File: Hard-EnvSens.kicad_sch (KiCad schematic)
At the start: 32 parts, among them P1 USB_C_Plug_USB2.0, SW1 SW_Push, SW3 SW_Push, U1 LD1117S33TR_SOT223, U2 ESP32-C6-WROOM-1, U3 CP2104

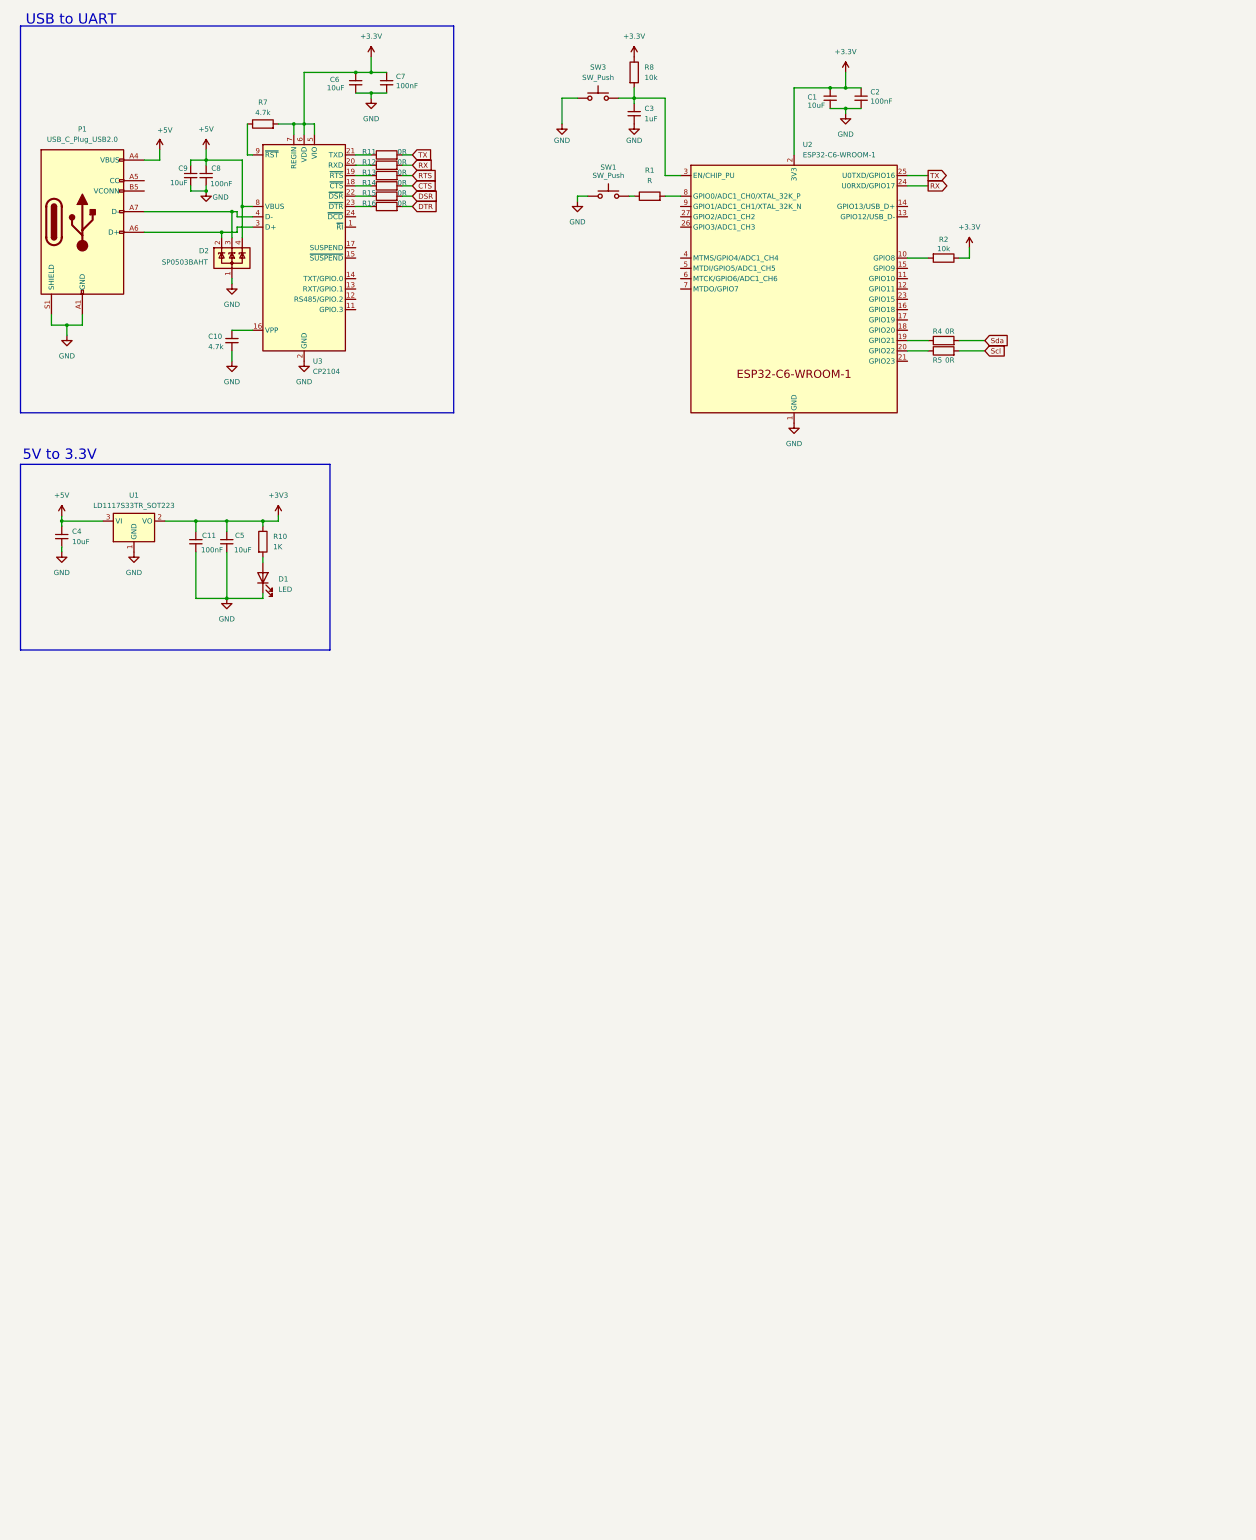
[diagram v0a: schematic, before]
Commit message: Added some sensors
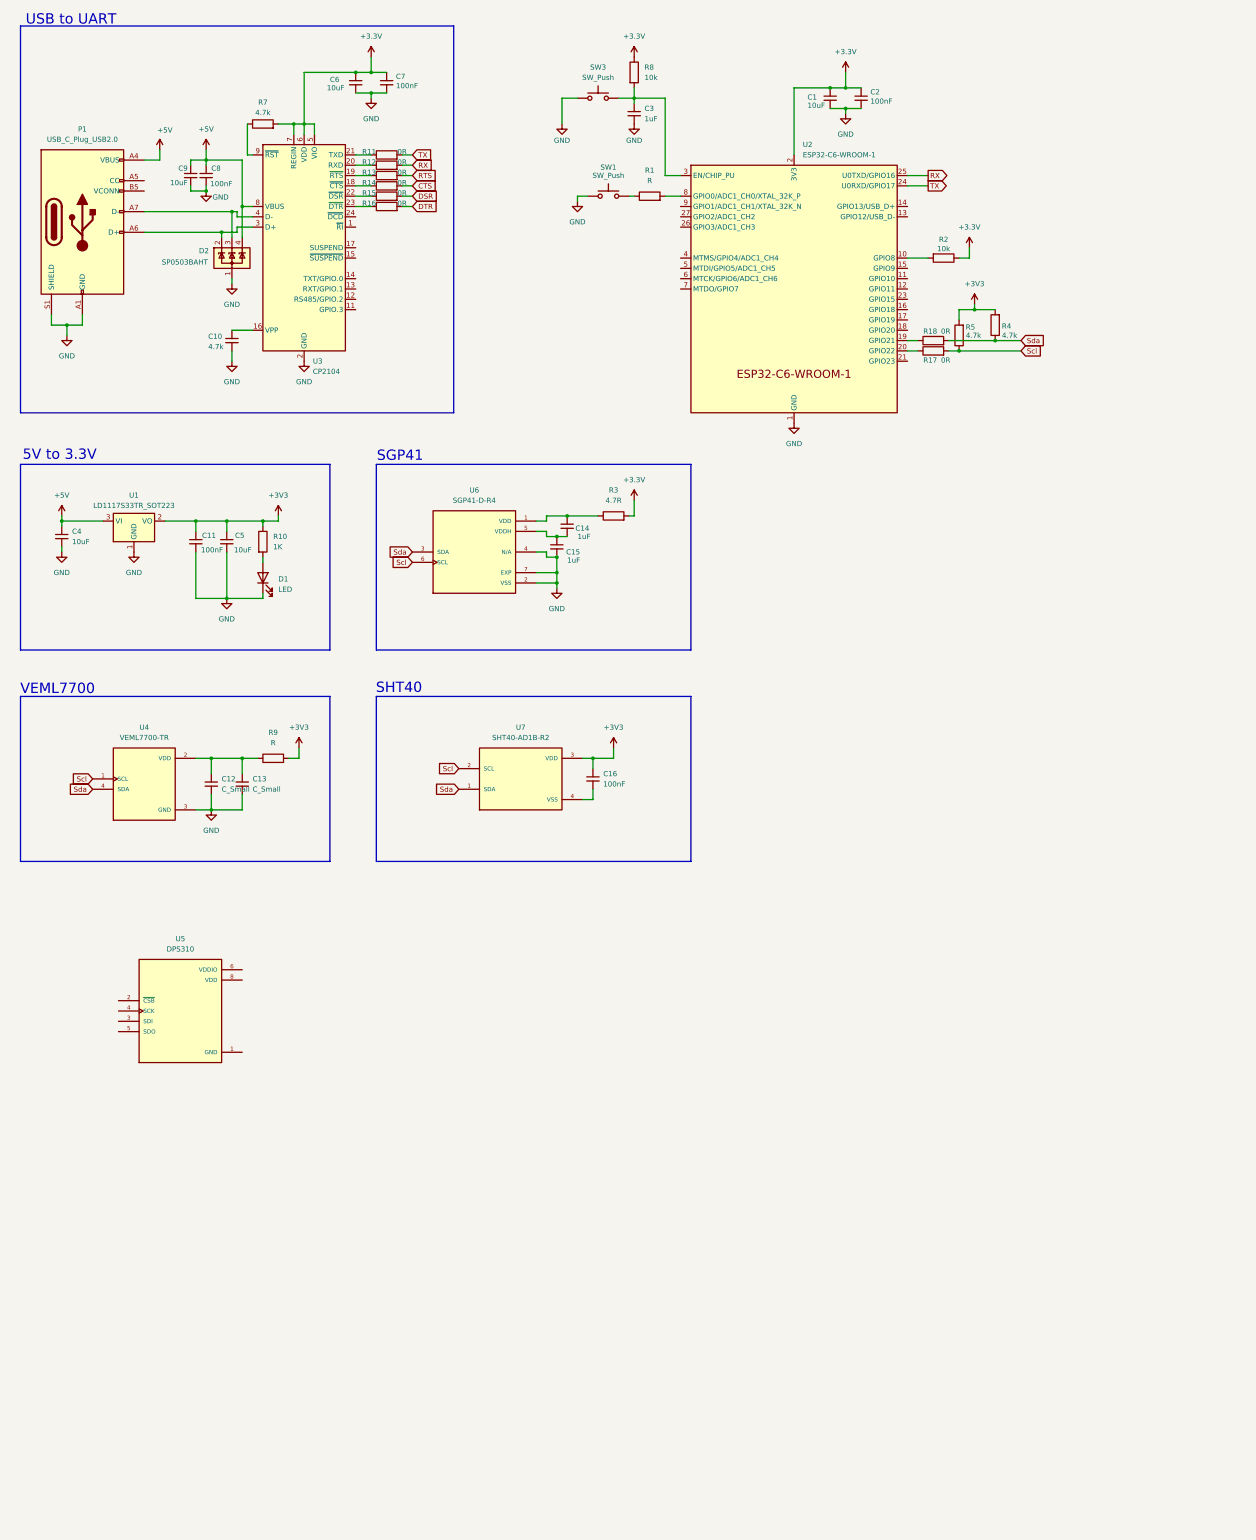
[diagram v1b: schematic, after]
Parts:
- added C12, C13: C_Small, symbol Device:C_Small
- added C14, C15: 1uF, symbol Device:C_Small
- added C16: 100nF, symbol Device:C_Small
- added R17, R18: 0R, symbol Device:R
- added R3: 4.7R, symbol Device:R
- added R9: R, symbol Device:R
- added U4: VEML7700-TR, VEML7700-TR:XDCR_VEML7700-TR, symbol VEML7700-TR:VEML7700-TR
- added U5: DPS310, DPS310:XDCR_DPS310, symbol DPS310:DPS310
- added U6: SGP41-D-R4, SGP41-D-R4:XDCR_SGP41-D-R4, symbol SGP41-D-R4:SGP41-D-R4
- added U7: SHT40-AD1B-R2, SHT40-AD1B-R2:SHT4X, symbol SHT40-AD1B-R2:SHT40-AD1B-R2
- R4, R5: value 0R -> 4.7k
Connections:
- net +3.3V: now also R3.2
- net +3V3: now also R4.2, R5.2, C16.1, R9.2, U7.3 (VDD)
- net GND: now also C12.2, C13.2, C15.2, U4.3 (GND), U5.1 (GND), U5.7 (GND), U6.2 (VSS), U6.4 (N/A), U6.7 (EXP)
- net RX: now also U2.25 (U0TXD/GPIO16); no longer U2.24 (U0RXD/GPIO17)
- net Scl: now also R5.1, R17.2, U4.1 (SCL), U6.6 (SCL), U7.2 (SCL); no longer R5.2
- net Sda: now also R4.1, R18.2, U4.4 (SDA), U6.3 (SDA), U7.1 (SDA); no longer R4.2
- net TX: now also U2.24 (U0RXD/GPIO17); no longer U2.25 (U0TXD/GPIO16)
- net at U2.20 (GPIO22): now also R17.1; no longer R5.1
- net at U2.19 (GPIO21): now also R18.1; no longer R4.1
- new net: C12.1, C13.1, R9.1, U4.2 (VDD)
- new net: C16.2, U7.4 (VSS)
- new net: C14.1, R3.1, U6.1 (VDD)
- new net: C14.2, C15.1, U6.5 (VDDH)
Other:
- note added: "SGP41"
- note added: "SHT40"
- note added: "VEML7700"
- moved on the sheet: R4, R5

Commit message: Dps368
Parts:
- removed R14, R16: 0R, symbol Device:R
- added C17: 10nF, symbol Device:C_Small
- added D3: SP0503BAHT, Package_TO_SOT_SMD:SOT-143, symbol Power_Protection:SP0503BAHT
- added D4: LED, symbol Device:LED
- added P2: USB_C_Plug_USB2.0, symbol Connector:USB_C_Plug_USB2.0
- added Q1, Q2: SS8050, Package_TO_SOT_SMD:SOT-23, symbol Transistor_BJT:SS8050
- added R19, R6: 12k, symbol Device:R
- R1: value R -> 10k
- R11, R12: value 0R -> 100R
- R13: value 0R -> 4.7k
- R9: value R -> 10R
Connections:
- net +3.3V: now also R1.1
- net +5V: now also D3.4 (K), P2.A4 (VBUS), P2.A9 (VBUS), P2.B4 (VBUS), P2.B9 (VBUS)
- net DTR: now also U3.23 (~{DTR}), Q2.2 (E), R6.2
- net GND: now also D3.1 (A), D4.1 (K), P2.A1 (GND), P2.A12 (GND), P2.B1 (GND), P2.B12 (GND), P2.S1 (SHIELD)
- net RTS: now also U3.19 (~{RTS}), Q1.2 (E), R19.1; no longer R13.2
- net EN: now reaches C3.1, R8.2, SW3.2, U2.3 (EN/CHIP_PU)
- net EN: now also Q1.3 (C)
- net at SW1.2: now also R1.2, U2.8 (GPIO0/ADC1_CH0/XTAL_32K_P); no longer R1.1
- net at C14.1, R3.1, U6.1 (VDD): now also C17.1
- net at R13.1: now also D4.2 (A); no longer U3.19 (~{RTS})
- net at C14.2, C15.1, U6.5 (VDDH): now also C17.2
- net D-: now reaches U2.13 (GPIO12/USB_D-)
- net D-: now also D3.3 (K), P2.A7 (D-)
- net D+: now reaches U2.14 (GPIO13/USB_D+)
- net D+: now also D3.2 (K), P2.A6 (D+)
- net IO9: now reaches U2.15 (GPIO9)
- net IO9: now also Q2.3 (C)
- net at U2.23 (GPIO15): now also R13.2
- new net: Q2.1 (B), R19.2
- new net: Q1.1 (B), R6.1
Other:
- moved on the sheet: C1, C11, C12, C13, C14, C15, C16, C2, C3, C4, C5, D1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

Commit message: dps368
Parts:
- removed U5: DPS310, DPS310:XDCR_DPS310, symbol DPS310:DPS310
- added C18, C19: 100nF, symbol Device:C_Small
- added U5: DPS368, DPS368:LGA8S145X65P2X4_200X250X110-V, symbol DPS368:DPS368
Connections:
- net GND: now also C18.2, C19.2, U5.1 (GND_1), U5.7 (GND_2)
- net Scl: now also U5.4 (SCK)
- net Sda: now also U5.3 (SDI)
- new net: C18.1, C19.1, U5.6 (VDDIO), U5.8 (VDD)
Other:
- note added: "Debug USB"
- moved on the sheet: D3, P2

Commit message: aa
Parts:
- added U8: AS7341-DLGT, AS7341-DLGT:PSON80P310X200X110-8N, symbol AS7341-DLGT:AS7341-DLGT
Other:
- note added: "DPS368"
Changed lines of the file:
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@@
 		)
 	)
+	(text "DPS368\n"
+		(exclude_from_sim no)
+		(at 31.496 291.338 0)
+		(effects
+			(font
+				(size 2.54 2.54)
+			)
+		)
+	)
 	(text "5V to 3.3V\n"
 		(exclude_from_sim no)
@@
 					(unit 1)
 				)
+			)
+		)
+	)
+	(symbol
+		(lib_id "AS7341-DLGT:AS7341-DLGT")
+		(at 148.59 314.96 0)
+		(unit 1)
+		(exclude_from_sim no)
+		(in_bom yes)
+		(on_board yes)
+		(dnp no)
+		(fields_autoplaced yes)
+		(property "Reference" "U8"
+			(at 148.59 297.18 0)
+			(effects
+				(font
+					(size 1.27 1.27)
+				)
+			)
+		)
+		(property "Value" "AS7341-DLGT"
+			(at 148.59 299.72 0)
+			(effects
+				(font
+					(size 1.27 1.27)
+				)
+			)
+		)
+		(property "Footprint" "AS7341-DLGT:PSON80P310X200X110-8N"
+			(at 148.59 314.96 0)
+			(effects
+				(font
+					(size 1.27 1.27)
+				)
+				(justify bottom)
+				(hide yes)
+			)
+		)
+		(property "Datasheet" ""
+			(at 148.59 314.96 0)
+			(effects
+				(font
+					(size 1.27 1.27)
+				)
+				(hide yes)
+			)
+		)
+		(property "Description" ""
+			(at 148.59 314.96 0)
+			(effects
+				(font
+					(size 1.27 1.27)
+				)
+				(hide yes)
+			)
+		)
+		(property "MF" "ams"
+			(at 148.59 314.96 0)
+			(effects
+				(font
+					(size 1.27 1.27)
+				)
+				(justify bottom)
+				(hide yes)
+			)
+		)
+		(property "MAXIMUM_PACKAGE_HEIGHT" "1.1 mm"
+			(at 148.59 314.96 0)
+			(effects
+				(font
+					(size 1.27 1.27)
+				)
+				(justify bottom)
+				(hide yes)
+			)
+		)
+		(property "Package" "TFLGA-8 ams"
+			(at 148.59 314.96 0)
+			(effects
+				(font
+					(size 1.27 1.27)
+				)
+				(justify bottom)
+				(hide yes)
+			)
+		)
+		(property "Price" "None"
+			(at 148.59 314.96 0)
+			(effects
+				(font
+					(size 1.27 1.27)
+				)
+				(justify bottom)
+				(hide yes)
+			)
+		)
+		(property "Check_prices" "https://www.snapeda.com/parts/AS7341-DLGT/ams/view-part/?ref=eda"
+			(at 148.59 314.96 0)
+			(effects
+				(font
+					(size 1.27 1.27)
+				)
+				(justify bottom)
+				(hide yes)
+			)
+		)
+		(property "STANDARD" "IPC7351B"
+			(at 148.59 314.96 0)
+			(effects
+				(font
+					(size 1.27 1.27)
+				)
+				(justify bottom)
+				(hide yes)
+			)
+		)
+		(property "PARTREV" "V3"
+			(at 148.59 314.96 0)
+			(effects
+				(font
+					(size 1.27 1.27)
+				)
+				(justify bottom)
+				(hide yes)
+			)
+		)
+		(property "SnapEDA_Link" "https://www.snapeda.com/parts/AS7341-DLGT/ams/view-part/?ref=snap"
+			(at 148.59 314.96 0)
+			(effects
+				(font
+					(size 1.27 1.27)
+				)
+				(justify bottom)
+				(hide yes)
+			)
+		)
+		(property "MP" "AS7341-DLGT"
+			(at 148.59 314.96 0)
+			(effects
+				(font
+					(size 1.27 1.27)
+				)
+				(justify bottom)
+				(hide yes)
+			)
+		)
+		(property "Description_1" "Optical Sensor Ambient - I²C 8-TFLGA"
+			(at 148.59 314.96 0)
+			(effects
+				(font
+					(size 1.27 1.27)
+				)
+				(justify bottom)
+				(hide yes)
+			)
+		)
+		(property "Availability" "In Stock"
+			(at 148.59 314.96 0)
+			(effects
+				(font
+					(size 1.27 1.27)
+				)
+				(justify bottom)
+				(hide yes)
+			)
+		)
+		(property "MANUFACTURER" "AMS"
+			(at 148.59 314.96 0)
+			(effects
+				(font
+					(size 1.27 1.27)
+				)
+				(justify bottom)
+				(hide yes)
+			)
+		)
+		(pin "2"
+		)
+		(pin "6"
+		)
+		(pin "4"
+		)
+		(pin "8"
+		)
+		(pin "5"
+		)
+		(pin "3"
+		)
+		(pin "1"
+		)
+		(pin "7"
+		)
+		(instances
+			(project ""
+				(path "/08245449-9253-4ad9-82ff-78abebb7792e"
+					(reference "U8")
+					(unit 1)
+				)

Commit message: New sensors
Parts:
- removed R15: 0R, symbol Device:R
- added C20: 0.1uF, symbol Device:C_Small
- added C21: 0.01uF, symbol Device:C_Small
- added C22: 10uF, symbol Device:C_Small
- added C23: 100nF, symbol Device:C_Small
- added C24: 4.7uF, symbol Device:C_Small
- added R14: 10k, symbol Device:R
- added U9: TPS79318DBVTG4, TPS79318DBVTG4:SOT95P280X145-5N, symbol TPS793-18:TPS79318DBVTG4
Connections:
- net +5V: now also C20.1, U9.1 (IN), U9.3 (EN)
- net GND: now also U8.3 (GND), U8.5 (PGND), C20.2, C21.2, C22.2, C23.2, C24.2, U9.2 (GND)
- net Scl: now also U8.2 (SCL)
- net Sda: now also U8.8 (SDA)
- net 1.8v: now reaches U8.1 (VDD)
- net 1.8v: now also C22.1, C23.1, C24.1, R14.2, U9.5 (OUT)
- net at U8.7 (INT): now also R14.1
- new net: C21.1, U9.4 (NR)
- no-connect marks 0 -> 31
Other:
- moved on the sheet: C14, C15, C17, R3, U6, U8

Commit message: Sch done
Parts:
- U4: footprint VEML7700-TR:XDCR_VEML7700-TR -> Biblioteca_Kicad:XDCR_VEML7700-TR
- U5: footprint DPS368:LGA8S145X65P2X4_200X250X110-V -> Biblioteca_Kicad:LGA8S145X65P2X4_200X250X110-V
- U6: footprint SGP41-D-R4:XDCR_SGP41-D-R4 -> Biblioteca_Kicad:XDCR_SGP41-D-R4
- U7: footprint SHT40-AD1B-R2:SHT4X -> Biblioteca_Kicad:SHT4X
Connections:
- net +3.3V is gone; now on net +3V3: C1.1, C2.1, C6.1, C7.1, R1.1, R2.1, R3.2, R7.2, R8.1, U2.2 (3V3), U3.5 (VIO), U3.6 (VDD), U3.7 (REGIN)
- net +3V3: now also C15.1, C18.1, C19.1, U5.6 (VDDIO), U5.8 (VDD), U6.5 (VDDH)
- net GND: now also C14.2, C16.2, C17.2, U7.4 (VSS)
- net 1.8v renamed +1V8
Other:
- moved on the sheet: C1, C15, C18, C19, C2, C3, D4, Q1, Q2, R1, R13, R17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
